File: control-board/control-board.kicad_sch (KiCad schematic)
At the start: 95 parts, among them J1 Conn_01x03, J10 DIN-4, J11 DIN-4, J12 Conn_01x03, J13 Conn_01x03, J14 Conn_01x02, J15 Conn_01x03, J16 Conn_01x02, J17 Conn_01x02, J18 Conn_01x02, J2 GPS_ANT, J3 LORA_ANT, J4 DIN-4, J5 DIN-4, J6 USB_C_Receptacle_USB2.0_16P, J7 Conn_01x03, J8 DIN-4, J9 DIN-4, Q1 2N7002, Q2 2N7002, SW1 SW_SPST, U1 STM32H743VITx, U2 NEO-XM, U3 TCAN1462VDRQ1, U4 AMS1117-3.3, U6 AMS1117-3.3, U7 TCAN1462VDRQ1, Y1 8M, Y2 32.768k

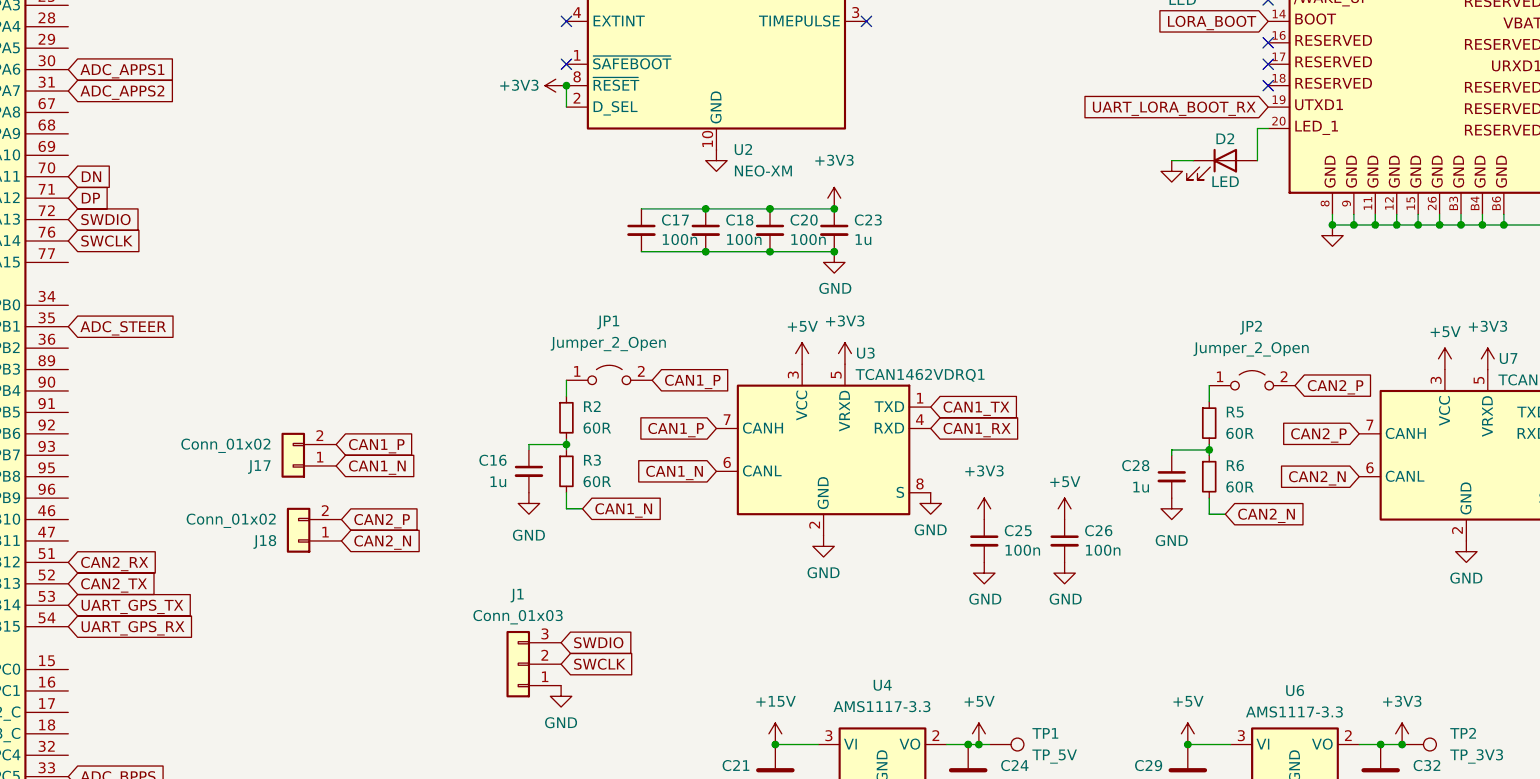
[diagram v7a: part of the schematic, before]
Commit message: feat: add ESD in CAN
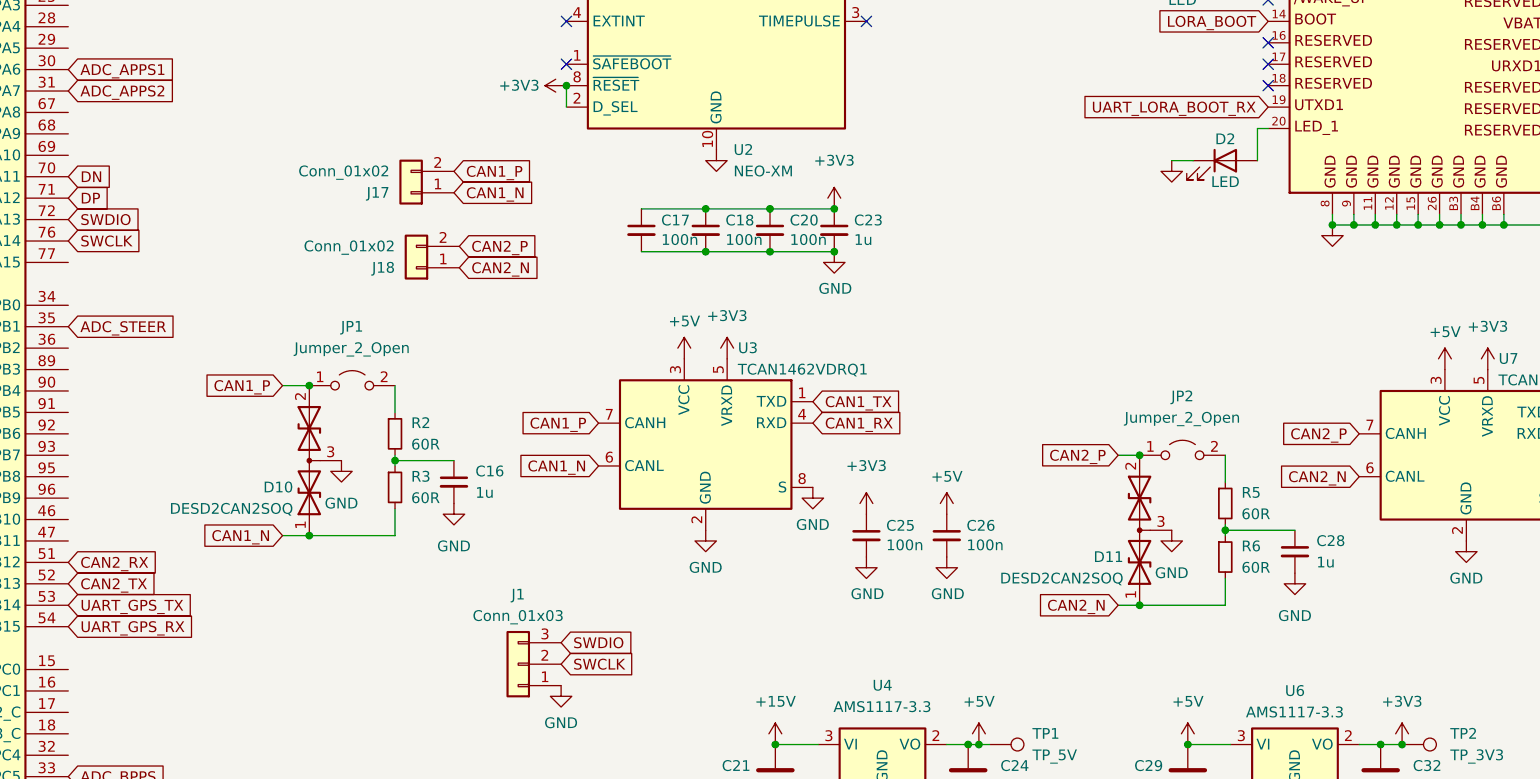
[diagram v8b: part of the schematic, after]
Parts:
- added D10, D11: DESD2CAN2SOQ, Package_TO_SOT_SMD:TSOT-23, symbol Device:D_TVS_Dual_AAC
- JP1, JP2: footprint Connector_PinHeader_2.54mm:PinHeader_1x02_P2.54mm_Vertical -> TestPoint:TestPoint_2Pads_Pitch2.54mm_Drill0.8mm
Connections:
- net CAN1_N: now also D10.1 (A1)
- net CAN1_P: now also JP1.1 (A), D10.2 (A2); no longer JP1.2 (B)
- net CAN2_N: now also D11.1 (A1)
- net CAN2_P: now also JP2.1 (A), D11.2 (A2); no longer JP2.2 (B)
- net GND: now also D10.3 (common), D11.3 (common)
- net at R2.1: now also JP1.2 (B); no longer JP1.1 (A)
- net at R5.1: now also JP2.2 (B); no longer JP2.1 (A)
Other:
- moved on the sheet: C16, C25, C26, C28, J17, J18, R2, R3, R5, R6, U3
